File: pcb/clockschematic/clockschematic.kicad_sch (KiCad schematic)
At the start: 19 parts, among them SW1 SW_Push, SW2 SW_Push, SW3 SW_Push, SW4 SW_Push, U0 RPi_Pico_TH, U1 RDA5807M_Module, U2 LM386, U3 LM386

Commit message: update
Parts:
- added J1: Barrel_Jack, Connector_BarrelJack:BarrelJack_CUI_PJ-063AH_Horizontal, symbol Connector:Barrel_Jack
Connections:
- net +3.3V: no longer U2.6 (V+), U3.6 (V+)
- net GND: now also J1.2
- net +5V: now reaches U0.40 (VBUS)
- net +5V: now also U2.6 (V+), U3.6 (V+), J1.1
- no-connect marks 35 -> 34
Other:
- moved on the sheet: C1, C2, C3, C4, DISP1, LS1, LS2, R1, R2, R3, R4, SW1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

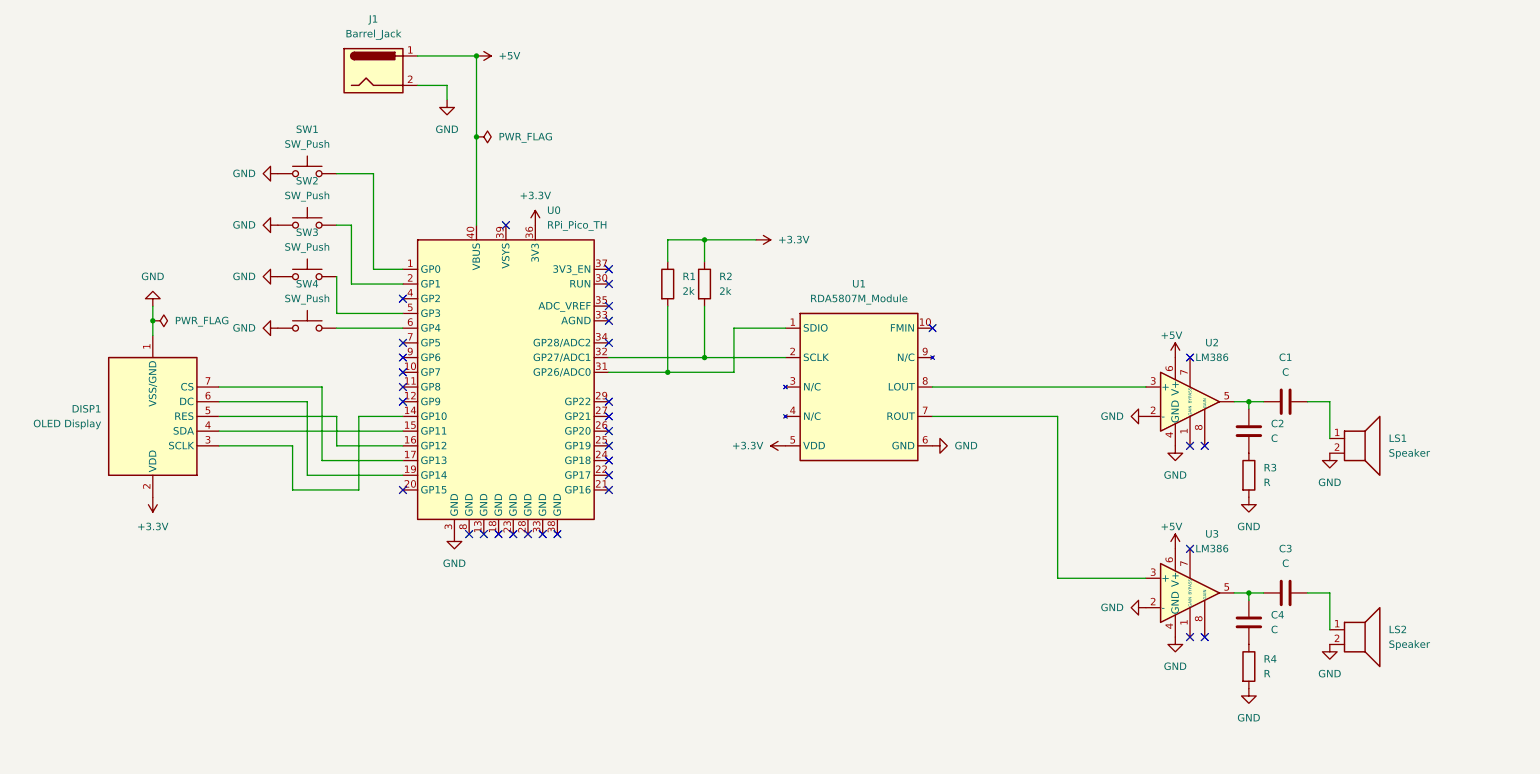
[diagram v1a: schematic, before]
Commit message: time is working display is working radio is working new pcb
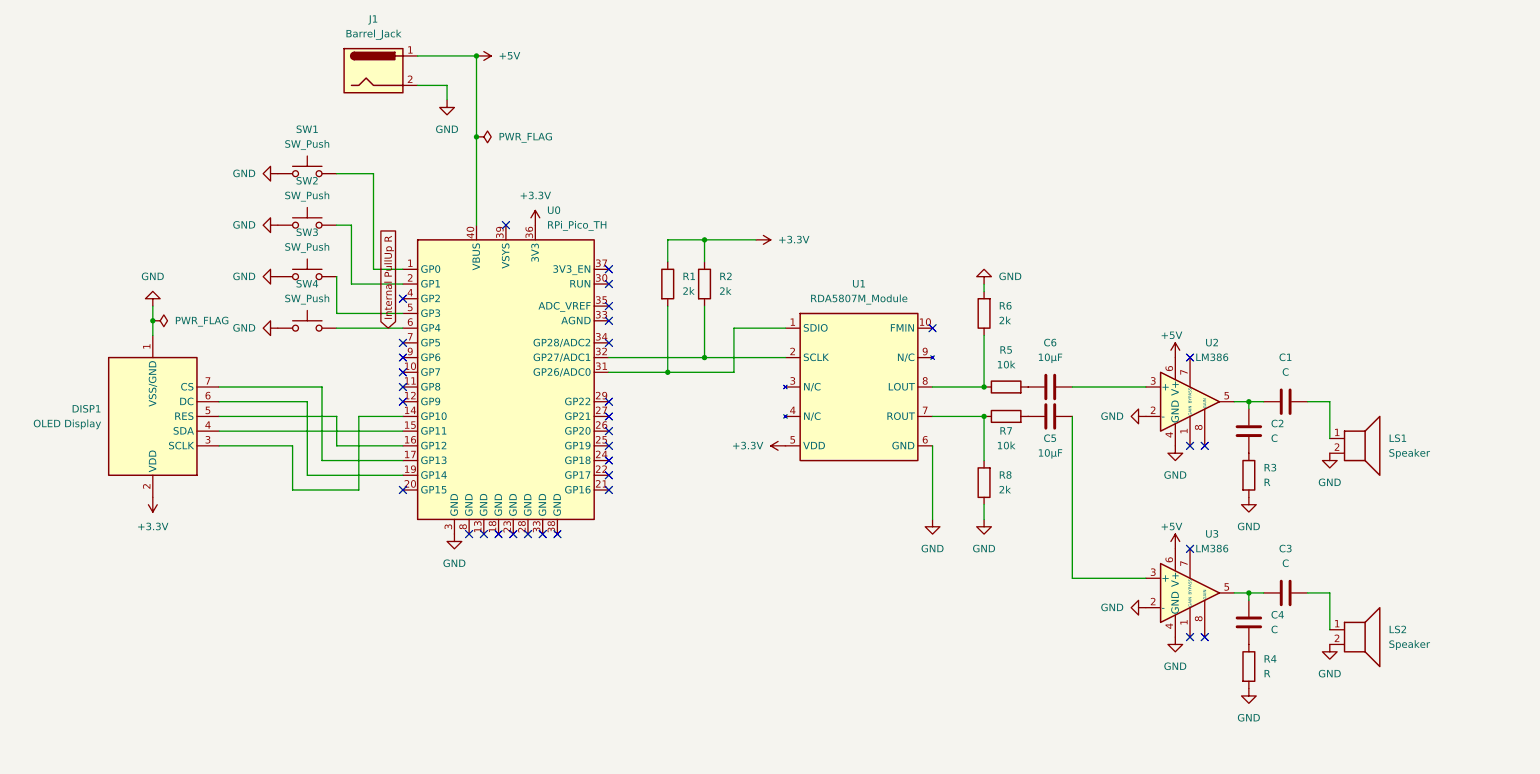
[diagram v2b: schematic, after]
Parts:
- added C5, C6: 10µF, Capacitor_THT:CP_Radial_D4.0mm_P2.00mm, symbol Device:C
- added R5, R7: 10k, Resistor_THT:R_Axial_DIN0204_L3.6mm_D1.6mm_P7.62mm_Horizontal, symbol Device:R
- added R6, R8: 2k, Resistor_THT:R_Axial_DIN0204_L3.6mm_D1.6mm_P7.62mm_Horizontal, symbol Device:R
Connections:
- net GND: now also R6.2, R8.1
- net at U1.7 (ROUT): now also R7.1, R8.2; no longer U3.3 (+)
- net at U1.8 (LOUT): now also R5.1, R6.1; no longer U2.3 (+)
- net Internal PullUp R: now reaches SW4.2, U0.6 (GP4)
- new net: C5.1, R7.2
- new net: C5.2, U3.3 (+)
- new net: C6.2, U2.3 (+)
- new net: C6.1, R5.2
